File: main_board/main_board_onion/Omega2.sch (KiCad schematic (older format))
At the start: 27 parts, among them J10 RJ45, J11 USB_B_Micro_Omega, Q1 BSS138, U3 H1102, U4 CP2102N-A01-GQFN24

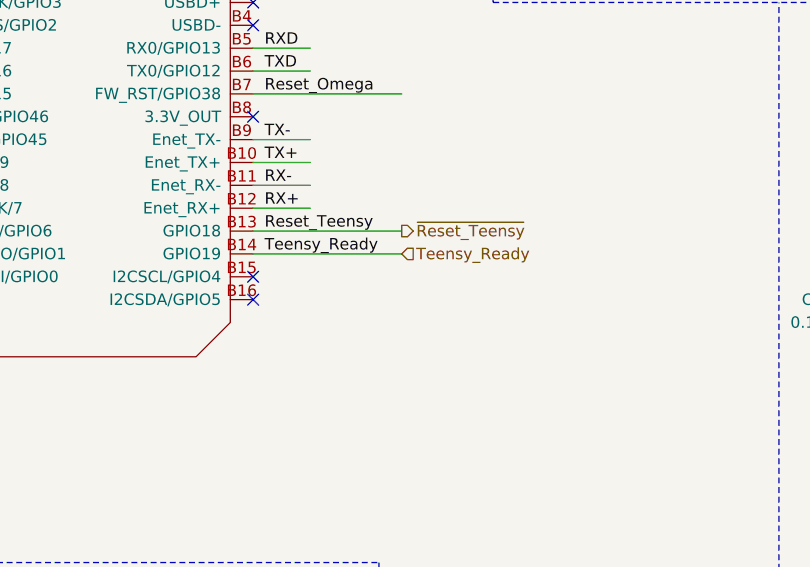
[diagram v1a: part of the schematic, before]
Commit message: Added new nRF24 library
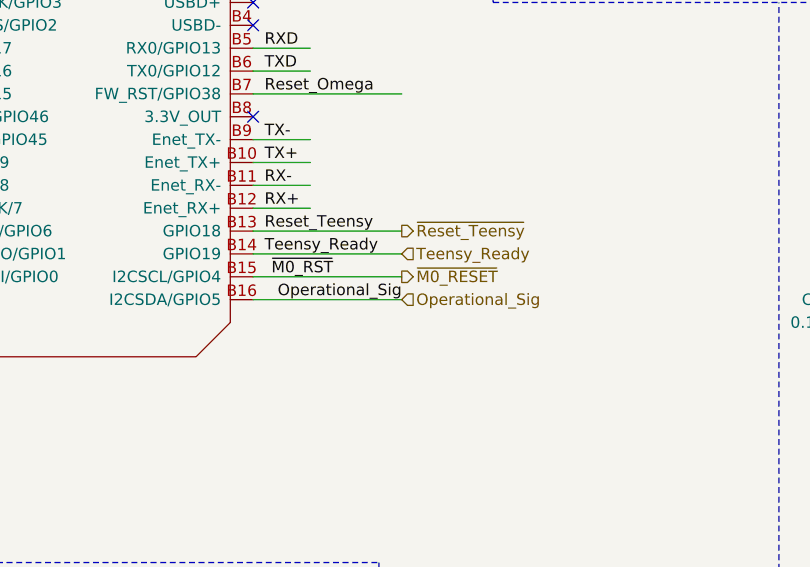
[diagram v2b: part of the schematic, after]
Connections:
- net labels added: Operational_Sig, ~M0_RESET, ~M0_RST
- wire segments 128 -> 130
- no-connect marks 35 -> 33
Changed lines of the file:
@@
 NoConn ~ 5000 3350
 NoConn ~ 5000 3450
-NoConn ~ 6450 3450
-NoConn ~ 6450 3550
 Wire Wire Line
 	6450 2650 7100 2650
@@
 Text Label 10100 5450 2    50   ~ 0
 ResetGate
+Text Label 6800 3450 2    50   ~ 0
+~M0_RST
+Text Label 7100 3550 2    50   ~ 0
+Operational_Sig
+Text HLabel 7100 3450 2    50   Output ~ 0
+~M0_RESET
+Text HLabel 7100 3550 2    50   Input ~ 0
+Operational_Sig
+Wire Wire Line
+	6450 3450 7100 3450
+Wire Wire Line
+	6450 3550 7100 3550
 $EndSCHEMATC

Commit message: Started placing Onion USB, 5v, 3v3 power.
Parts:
- removed D1: CLV1L-FKB, LED_SMD:LED_Cree-PLCC4_3.2x2.8mm_CCW, symbol LED:CLV1L-FKB
- removed R7, R8, R9: 1k, Resistor_SMD:R_0603_1608Metric, symbol Device:R
- C2, C3, C4, C5: footprint Capacitor_SMD:C_0603_1608Metric -> Capacitor_SMD:C_0402_1005Metric
- R1, R2, R3, R4, R5, R6: footprint Resistor_SMD:R_0603_1608Metric -> Resistor_SMD:R_0402_1005Metric
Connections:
- net labels removed: B_LED, G_LED, R_LED
- wire segments 130 -> 120
- no-connect marks 33 -> 36
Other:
- note added: "Omega Reset\n"
- note removed: "Add Extra antenna?"
- note removed: "RGB LED"
- moved on the sheet: Q1, R11
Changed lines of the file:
@@
 Wire Notes Line
 	8950 500  8950 2250
-Wire Notes Line
-	8750 4900 8750 2250
 Text Label 10300 4800 0    50   ~ 0
 PC_TXD
@@
 	6450 2550 6700 2550
 $Comp
-L LED:CLV1L-FKB D1
-U 1 1 5B6A8E1C
-P 8450 1350
-F 0 "D1" H 8450 1847 50  0000 C CNN
-F 1 "CLV1L-FKB" H 8450 1756 50  0000 C CNN
-F 2 "LED_SMD:LED_Cree-PLCC4_3.2x2.8mm_CCW" H 8450 1300 50  0001 C CNN
-F 3 "http://www.cree.com/led-components/media/documents/CLV1L-FKB-1238.pdf" H 8450 1300 50  0001 C CNN
-	1    8450 1350
-	1    0    0    -1
-$EndComp
-Wire Wire Line
-	8650 1350 8850 1350
-Text Label 8700 1350 0    50   ~ 0
-3v3
-$Comp
-L Device:R R7
-U 1 1 5B6AA8B8
-P 8000 1150
-F 0 "R7" V 7900 1150 50  0000 C CNN
-F 1 "1k" V 8000 1150 50  0000 C CNN
-F 2 "Resistor_SMD:R_0603_1608Metric" V 7930 1150 50  0001 C CNN
-F 3 "~" H 8000 1150 50  0001 C CNN
-	1    8000 1150
-	0    1    1    0
-$EndComp
-$Comp
-L Device:R R8
-U 1 1 5B6AA9DD
-P 8000 1350
-F 0 "R8" V 7900 1350 50  0000 C CNN
-F 1 "1k" V 8000 1350 50  0000 C CNN
-F 2 "Resistor_SMD:R_0603_1608Metric" V 7930 1350 50  0001 C CNN
-F 3 "~" H 8000 1350 50  0001 C CNN
-	1    8000 1350
-	0    1    1    0
-$EndComp
-$Comp
-L Device:R R9
-U 1 1 5B6AAA0D
-P 8000 1550
-F 0 "R9" V 7900 1550 50  0000 C CNN
-F 1 "1k" V 8000 1550 50  0000 C CNN
-F 2 "Resistor_SMD:R_0603_1608Metric" V 7930 1550 50  0001 C CNN
-F 3 "~" H 8000 1550 50  0001 C CNN
-	1    8000 1550
-	0    1    1    0
-$EndComp
-Wire Wire Line
-	8150 1550 8250 1550
-Wire Wire Line
-	8150 1350 8250 1350
-Wire Wire Line
-	8150 1150 8250 1150
-Text Label 4950 2650 2    50   ~ 0
-R_LED
-Text Label 4950 2550 2    50   ~ 0
-G_LED
-Text Label 4950 2450 2    50   ~ 0
-B_LED
-Wire Wire Line
-	5000 2450 4700 2450
-Wire Wire Line
-	5000 2550 4700 2550
-Wire Wire Line
-	5000 2650 4700 2650
-Text Label 7600 1150 0    50   ~ 0
-R_LED
-Text Label 7600 1350 0    50   ~ 0
-G_LED
-Text Label 7600 1550 0    50   ~ 0
-B_LED
-Wire Wire Line
-	7550 1550 7850 1550
-Wire Wire Line
-	7550 1350 7850 1350
-Wire Wire Line
-	7550 1150 7850 1150
-Text Notes 8000 700  0    50   ~ 0
-RGB LED
-Wire Notes Line
-	7500 2250 7500 500
-Wire Notes Line
-	7500 2250 11200 2250
-$Comp
 L Pulse:H1102 U3
 U 1 1 5B6C2CE9
@@
 NoConn ~ 3800 7200
 NoConn ~ 3800 7100
-NoConn ~ 2450 7200
-NoConn ~ 2450 7100
 Wire Wire Line
 	5150 6550 4500 6550
@@
 F 0 "R5" H 4020 7346 50  0000 L CNN
 F 1 "75" H 4020 7255 50  0000 L CNN
-F 2 "Resistor_SMD:R_0603_1608Metric" V 3880 7300 50  0001 C CNN
+F 2 "Resistor_SMD:R_0402_1005Metric" V 3880 7300 50  0001 C CNN
 F 3 "~" H 3950 7300 50  0001 C CNN
 	1    3950 7300
@@
 F 0 "R6" H 4270 7346 50  0000 L CNN
 F 1 "75" H 4270 7255 50  0000 L CNN
-F 2 "Resistor_SMD:R_0603_1608Metric" V 4130 7300 50  0001 C CNN
+F 2 "Resistor_SMD:R_0402_1005Metric" V 4130 7300 50  0001 C CNN
 F 3 "~" H 4200 7300 50  0001 C CNN
 	1    4200 7300
@@
 F 0 "C5" V 5421 7600 50  0000 C CNN
 F 1 "1nF/2KV" V 5512 7600 50  0000 C CNN
-F 2 "Capacitor_SMD:C_0603_1608Metric" H 5650 7600 50  0001 C CNN
+F 2 "Capacitor_SMD:C_0402_1005Metric" H 5650 7600 50  0001 C CNN
 F 3 "~" H 5650 7600 50  0001 C CNN
 	1    5650 7600
@@
 F 0 "R1" H 1700 5550 50  0000 L CNN
 F 1 "49.9" H 1600 5450 50  0000 L CNN
-F 2 "Resistor_SMD:R_0603_1608Metric" V 1780 5500 50  0001 C CNN
+F 2 "Resistor_SMD:R_0402_1005Metric" V 1780 5500 50  0001 C CNN
 F 3 "~" H 1850 5500 50  0001 C CNN
 	1    1850 5500
@@
 F 0 "R3" H 2020 5546 50  0000 L CNN
 F 1 "49.9" H 2020 5455 50  0000 L CNN
-F 2 "Resistor_SMD:R_0603_1608Metric" V 1880 5500 50  0001 C CNN
+F 2 "Resistor_SMD:R_0402_1005Metric" V 1880 5500 50  0001 C CNN
 F 3 "~" H 1950 5500 50  0001 C CNN
 	1    1950 5500
@@
 F 0 "C2" V 1098 5050 50  0000 C CNN
 F 1 "100nF" V 1189 5050 50  0000 C CNN
-F 2 "Capacitor_SMD:C_0603_1608Metric" H 1388 4900 50  0001 C CNN
+F 2 "Capacitor_SMD:C_0402_1005Metric" H 1388 4900 50  0001 C CNN
 F 3 "~" H 1350 5050 50  0001 C CNN
 	1    1350 5050
@@
 F 0 "C4" H 2385 5254 50  0000 R CNN
 F 1 "1uF" H 2385 5345 50  0000 R CNN
-F 2 "Capacitor_SMD:C_0603_1608Metric" H 2538 5150 50  0001 C CNN
+F 2 "Capacitor_SMD:C_0402_1005Metric" H 2538 5150 50  0001 C CNN
 F 3 "~" H 2500 5300 50  0001 C CNN
 	1    2500 5300
@@
 F 0 "R2" H 1700 7250 50  0000 L CNN
 F 1 "49.9" H 1600 7150 50  0000 L CNN
-F 2 "Resistor_SMD:R_0603_1608Metric" V 1780 7200 50  0001 C CNN
+F 2 "Resistor_SMD:R_0402_1005Metric" V 1780 7200 50  0001 C CNN
 F 3 "~" H 1850 7200 50  0001 C CNN
 	1    1850 7200
@@
 F 0 "R4" H 2020 7246 50  0000 L CNN
 F 1 "49.9" H 2020 7155 50  0000 L CNN
-F 2 "Resistor_SMD:R_0603_1608Metric" V 1880 7200 50  0001 C CNN
+F 2 "Resistor_SMD:R_0402_1005Metric" V 1880 7200 50  0001 C CNN
 F 3 "~" H 1950 7200 50  0001 C CNN
 	1    1950 7200
@@
 F 0 "C3" V 1602 7650 50  0000 C CNN
 F 1 "100nF" V 1511 7650 50  0000 C CNN
-F 2 "Capacitor_SMD:C_0603_1608Metric" H 1388 7500 50  0001 C CNN
+F 2 "Capacitor_SMD:C_0402_1005Metric" H 1388 7500 50  0001 C CNN
 F 3 "~" H 1350 7650 50  0001 C CNN
 	1    1350 7650
@@
 Text HLabel 7100 3250 2    50   Output ~ 0
 ~Reset_Teensy
-Text Notes 5100 1200 0    98   ~ 0
-Add Extra antenna?
 $Comp
 L Connector:RJ45 J10
@@
 VDD25
 Wire Wire Line
-	9200 5925 8600 5925
-Wire Wire Line
-	9575 5250 9575 5175
-Wire Wire Line
-	9575 5175 9925 5175
-Wire Wire Line
-	9500 5925 9575 5925
-Wire Wire Line
-	9575 5925 9575 5650
+	9575 6100 8975 6100
+Wire Wire Line
+	9950 5425 9950 5350
+Wire Wire Line
+	9950 5350 10300 5350
+Wire Wire Line
+	9875 6100 9950 6100
+Wire Wire Line
+	9950 6100 9950 5825
 $Comp
 L Device:R R11
 U 1 1 5D0274A7
-P 9350 5925
-F 0 "R11" V 9143 5925 50  0000 C CNN
-F 1 "330" V 9234 5925 50  0000 C CNN
-F 2 "Resistor_SMD:R_0603_1608Metric" V 9280 5925 50  0001 C CNN
-F 3 "~" H 9350 5925 50  0001 C CNN
-	1    9350 5925
+P 9725 6100
+F 0 "R11" V 9518 6100 50  0000 C CNN
+F 1 "330" V 9609 6100 50  0000 C CNN
+F 2 "Resistor_SMD:R_0603_1608Metric" V 9655 6100 50  0001 C CNN
+F 3 "~" H 9725 6100 50  0001 C CNN
+	1    9725 6100
 	0    1    1    0
 $EndComp
@@
 L Transistor_FET:BSS138 Q1
 U 1 1 5D02392E
-P 9675 5450
-F 0 "Q1" H 9881 5496 50  0000 L CNN
-F 1 "BSS138" H 9881 5405 50  0000 L CNN
-F 2 "Package_TO_SOT_SMD:SOT-23" H 9875 5375 50  0001 L CIN
-F 3 "https://www.fairchildsemi.com/datasheets/BS/BSS138.pdf" H 9675 5450 50  0001 L CNN
-	1    9675 5450
+P 10050 5625
+F 0 "Q1" H 10256 5671 50  0000 L CNN
+F 1 "BSS138" H 10256 5580 50  0000 L CNN
+F 2 "Package_TO_SOT_SMD:SOT-23" H 10250 5550 50  0001 L CIN
+F 3 "https://www.fairchildsemi.com/datasheets/BS/BSS138.pdf" H 10050 5625 50  0001 L CNN
+	1    10050 5625
 	-1   0    0    -1
 $EndComp
-Text Label 9125 5925 2    50   ~ 0
+Text Label 9500 6100 2    50   ~ 0
 Reset_Omega
 Wire Wire Line
-	9875 5450 10150 5450
-Text Label 9850 5175 2    50   ~ 0
+	10250 5625 10525 5625
+Text Label 10225 5350 2    50   ~ 0
 VDD25
-Text HLabel 10150 5450 2    50   Input ~ 0
+Text HLabel 10525 5625 2    50   Input ~ 0
 Omega_Reset
-Text Label 10100 5450 2    50   ~ 0
+Text Label 10475 5625 2    50   ~ 0
 ResetGate
 Text Label 6800 3450 2    50   ~ 0
@@
 Wire Wire Line
 	6450 3550 7100 3550
+NoConn ~ 2450 7200
+NoConn ~ 2450 7100
+Wire Notes Line
+	8750 2250 11200 2250
+Text Notes 9750 5125 0    50   ~ 0
+Omega Reset\n
+Wire Notes Line
+	8750 2250 8750 6525
+NoConn ~ 5000 2450
+NoConn ~ 5000 2550
+NoConn ~ 5000 2650
 $EndSCHEMATC

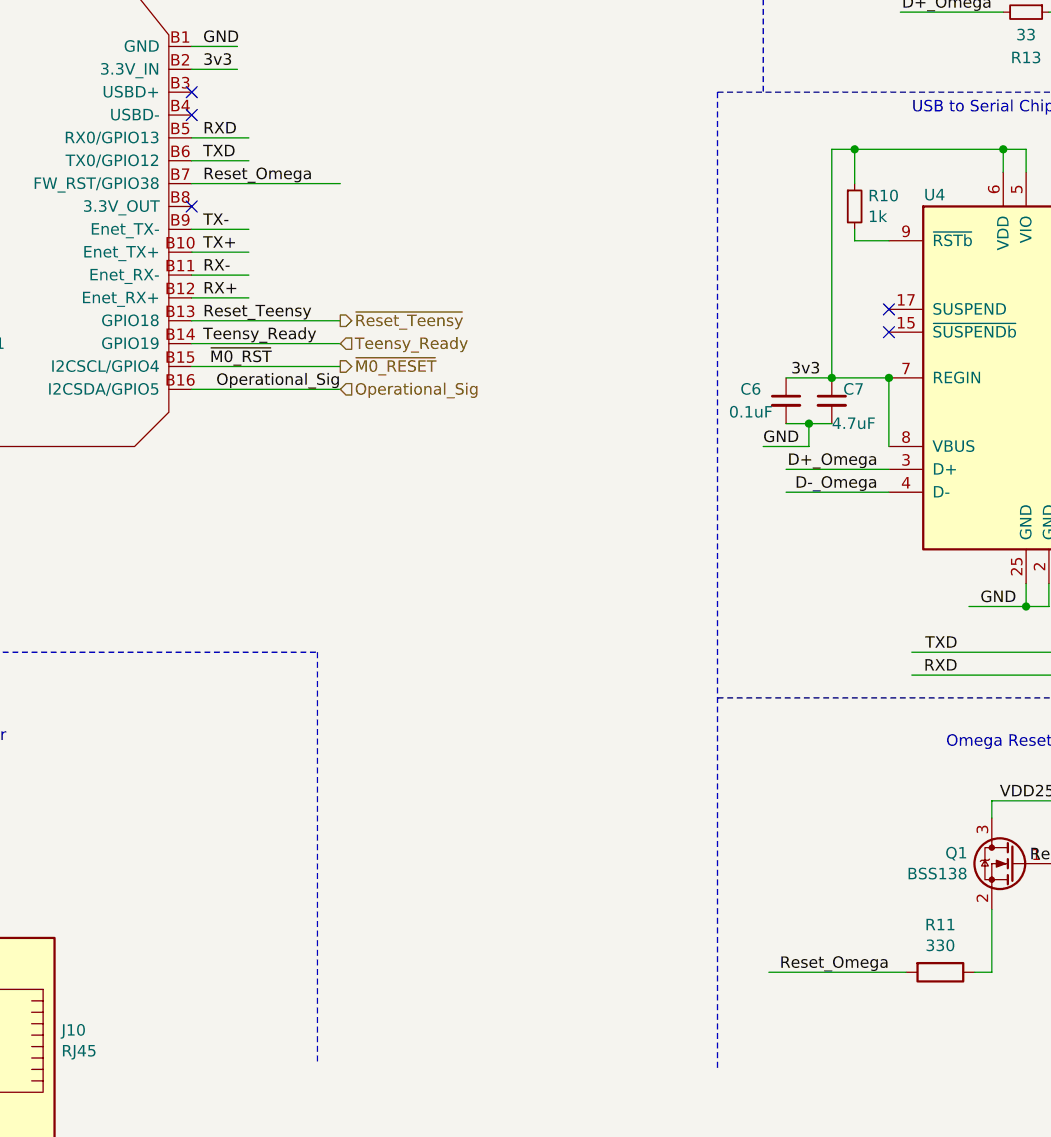
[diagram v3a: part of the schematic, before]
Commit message: Finished initial routing of this design
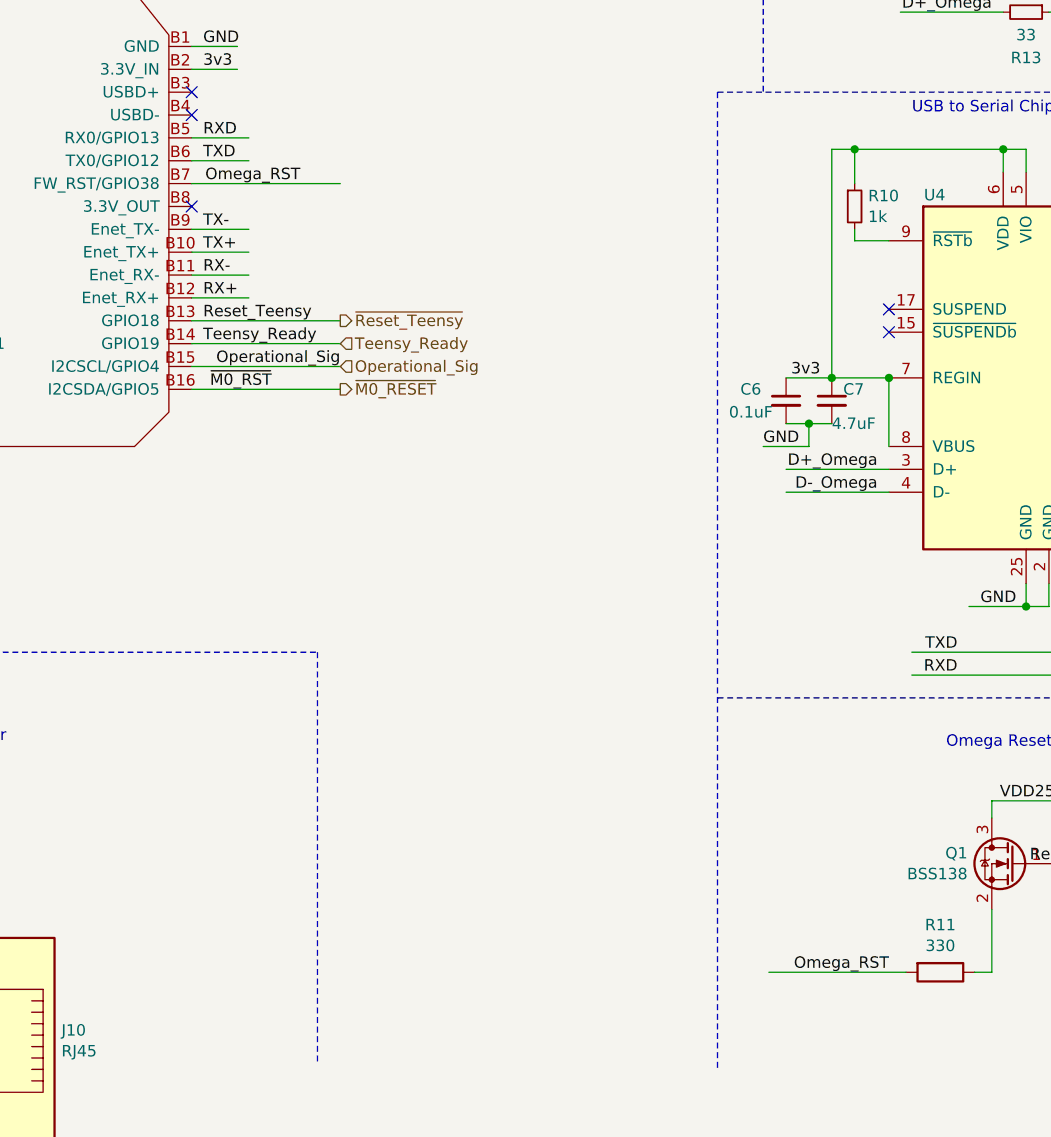
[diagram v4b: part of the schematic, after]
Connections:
- net labels added: Omega_RST
- net labels removed: Reset_Omega
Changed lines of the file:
@@
 Wire Wire Line
 	5000 2050 4800 2050
-Text Label 6500 2650 0    50   ~ 0
-Reset_Omega
+Text Label 6925 2650 2    50   ~ 0
+Omega_RST
 NoConn ~ 6450 2250
 NoConn ~ 6450 2350
@@
 $EndComp
 Text Label 9500 6100 2    50   ~ 0
-Reset_Omega
+Omega_RST
 Wire Wire Line
 	10250 5625 10525 5625
@@
 Text Label 10475 5625 2    50   ~ 0
 ResetGate
-Text Label 6800 3450 2    50   ~ 0
+Text Label 6800 3550 2    50   ~ 0
 ~M0_RST
-Text Label 7100 3550 2    50   ~ 0
+Text Label 7100 3450 2    50   ~ 0
 Operational_Sig
-Text HLabel 7100 3450 2    50   Output ~ 0
+Text HLabel 7100 3550 2    50   Output ~ 0
 ~M0_RESET
-Text HLabel 7100 3550 2    50   Input ~ 0
+Text HLabel 7100 3450 2    50   Input ~ 0
 Operational_Sig
 Wire Wire Line
+	6450 3550 7100 3550
+Wire Wire Line
 	6450 3450 7100 3450
-Wire Wire Line
-	6450 3550 7100 3550
 NoConn ~ 2450 7200
 NoConn ~ 2450 7100

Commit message: Added Gerber files for the version uploaded to MacroFab for manufacturing. Plus small changes made before uploading it.
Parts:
- C4: Field4 (none) -> MF-CAP-0402-1uF
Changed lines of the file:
@@
 F 2 "Capacitor_SMD:C_0402_1005Metric" H 1388 4900 50  0001 C CNN
 F 3 "~" H 1350 5050 50  0001 C CNN
+F 4 "" H 1350 5050 50  0001 C CNN "Manufacturer_Part_Number"
 	1    1350 5050
 	0    1    1    0
@@
 F 2 "Capacitor_SMD:C_0402_1005Metric" H 2538 5150 50  0001 C CNN
 F 3 "~" H 2500 5300 50  0001 C CNN
+F 4 "" H 2500 5300 50  0001 C CNN "Mouser Part Number"
+F 5 "" H 2500 5300 50  0001 C CNN "Description"
+F 6 "MF-CAP-0402-1uF" H 2500 5300 50  0001 C CNN "Field4"
 	1    2500 5300
 	-1   0    0    1
@@
 F 2 "Capacitor_SMD:C_0402_1005Metric" H 1388 7500 50  0001 C CNN
 F 3 "~" H 1350 7650 50  0001 C CNN
+F 4 "" H 1350 7650 50  0001 C CNN "Manufacturer_Part_Number"
 	1    1350 7650
 	0    1    -1   0
